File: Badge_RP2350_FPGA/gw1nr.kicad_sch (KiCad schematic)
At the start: 23 parts, among them U2 GW1N-LV9QN88C6_I5_, U6 W25Q32JVSS

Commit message: modify usb and flash connections
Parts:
- added R19: 4.7K, Resistor_THT:R_Axial_DIN0204_L3.6mm_D1.6mm_P1.90mm_Vertical, symbol Device:R
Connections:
- net GND: now also R19.1
- net TCK: now also R19.2
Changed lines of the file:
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@@
 		(rev "v1.0")
 		(company "SemiTO-V, RISC-V Student Team")
-		(comment 3 "License: CERN-OHL-W")
+		(comment 3 "License: CERN-OHL-W-2.0")
 		(comment 4 "Authors: Tan Siret Akıncı, Alessandro Bochino, Carlo Bendelli, Arianna Bruno")
 	)
@@
 	(wire
 		(pts
+			(xy 77.47 80.01) (xy 77.47 83.82)
+		)
+		(stroke
+			(width 0)
+			(type default)
+		)
+	)
+	(wire
+		(pts
 			(xy 166.37 43.18) (xy 179.07 43.18)
 		)
@@
 	(wire
 		(pts
+			(xy 77.47 68.58) (xy 77.47 72.39)
+		)
+		(stroke
+			(width 0)
+			(type default)
+		)
+	)
+	(wire
+		(pts
 			(xy 237.49 34.29) (xy 237.49 44.45)
 		)
@@
 	(wire
 		(pts
-			(xy 86.36 68.58) (xy 100.33 68.58)
+			(xy 77.47 68.58) (xy 100.33 68.58)
 		)
 		(stroke
@@
 	)
 	(label "TCK"
-		(at 86.36 68.58 0)
+		(at 77.47 68.58 0)
 		(effects
 			(font
@@
 	)
 	(symbol
+		(lib_id "power:GND")
+		(at 77.47 83.82 0)
+		(unit 1)
+		(body_style 1)
+		(exclude_from_sim no)
+		(in_bom yes)
+		(on_board yes)
+		(in_pos_files yes)
+		(dnp no)
+		(property "Reference" "#PWR053"
+			(at 77.47 90.17 0)
+			(hide yes)
+			(show_name no)
+			(do_not_autoplace no)
+			(effects
+				(font
+					(size 1.27 1.27)
+				)
+			)
+		)
+		(property "Value" "GND"
+			(at 73.66 85.09 0)
+			(show_name no)
+			(do_not_autoplace no)
+			(effects
+				(font
+					(size 1.27 1.27)
+				)
+			)
+		)
+		(property "Footprint" ""
+			(at 77.47 83.82 0)
+			(hide yes)
+			(show_name no)
+			(do_not_autoplace no)
+			(effects
+				(font
+					(size 1.27 1.27)
+				)
+			)
+		)
+		(property "Datasheet" ""
+			(at 77.47 83.82 0)
+			(hide yes)
+			(show_name no)
+			(do_not_autoplace no)
+			(effects
+				(font
+					(size 1.27 1.27)
+				)
+			)
+		)
+		(property "Description" ""
+			(at 77.47 83.82 0)
+			(show_name no)
+			(do_not_autoplace no)
+			(effects
+				(font
+					(size 1.27 1.27)
+				)
+			)
+		)
+		(pin "1"
+		)
+		(instances
+			(project "Badge_RP2350_FPGA"
+				(path "/0ce87b49-0553-4a87-87c1-84e31180901e/2d8d0ad2-8268-4696-bbfb-79e633c29f55"
+					(reference "#PWR053")
+					(unit 1)
+				)
+			)
+		)
+	)
+	(symbol
 		(lib_id "Memory_Flash:W25Q32JVSS")
 		(at 245.11 132.08 0)
@@
 					(unit 1)
 				)
+			)
+		)
+	)
+	(symbol
+		(lib_id "Device:R")
+		(at 77.47 76.2 180)
+		(unit 1)
+		(body_style 1)
+		(exclude_from_sim no)
+		(in_bom yes)
+		(on_board yes)
+		(in_pos_files yes)
+		(dnp no)
+		(fields_autoplaced yes)
+		(property "Reference" "R19"
+			(at 80.01 74.9299 0)
+			(show_name no)
+			(do_not_autoplace no)
+			(effects
+				(font
+					(size 1.27 1.27)
+				)
+				(justify right)
+			)
+		)
+		(property "Value" "4.7K"
+			(at 80.01 77.4699 0)
+			(show_name no)
+			(do_not_autoplace no)
+			(effects
+				(font
+					(size 1.27 1.27)
+				)
+				(justify right)
+			)
+		)
+		(property "Footprint" "Resistor_THT:R_Axial_DIN0204_L3.6mm_D1.6mm_P1.90mm_Vertical"
+			(at 79.248 76.2 90)
+			(hide yes)
+			(show_name no)
+			(do_not_autoplace no)
+			(effects
+				(font
+					(size 1.27 1.27)
+				)
+			)
+		)
+		(property "Datasheet" ""
+			(at 77.47 76.2 0)
+			(hide yes)
+			(show_name no)
+			(do_not_autoplace no)
+			(effects
+				(font
+					(size 1.27 1.27)
+				)
+			)
+		)
+		(property "Description" "Resistor"
+			(at 77.47 76.2 0)
+			(hide yes)
+			(show_name no)
+			(do_not_autoplace no)
+			(effects
+				(font
+					(size 1.27 1.27)
+				)
+			)
+		)
+		(pin "1"
+		)
+		(pin "2"
+		)
+		(instances
+			(project "Badge_RP2350_FPGA"
+				(path "/0ce87b49-0553-4a87-87c1-84e31180901e/2d8d0ad2-8268-4696-bbfb-79e633c29f55"
+					(reference "R19")
+					(unit 1)
+				)

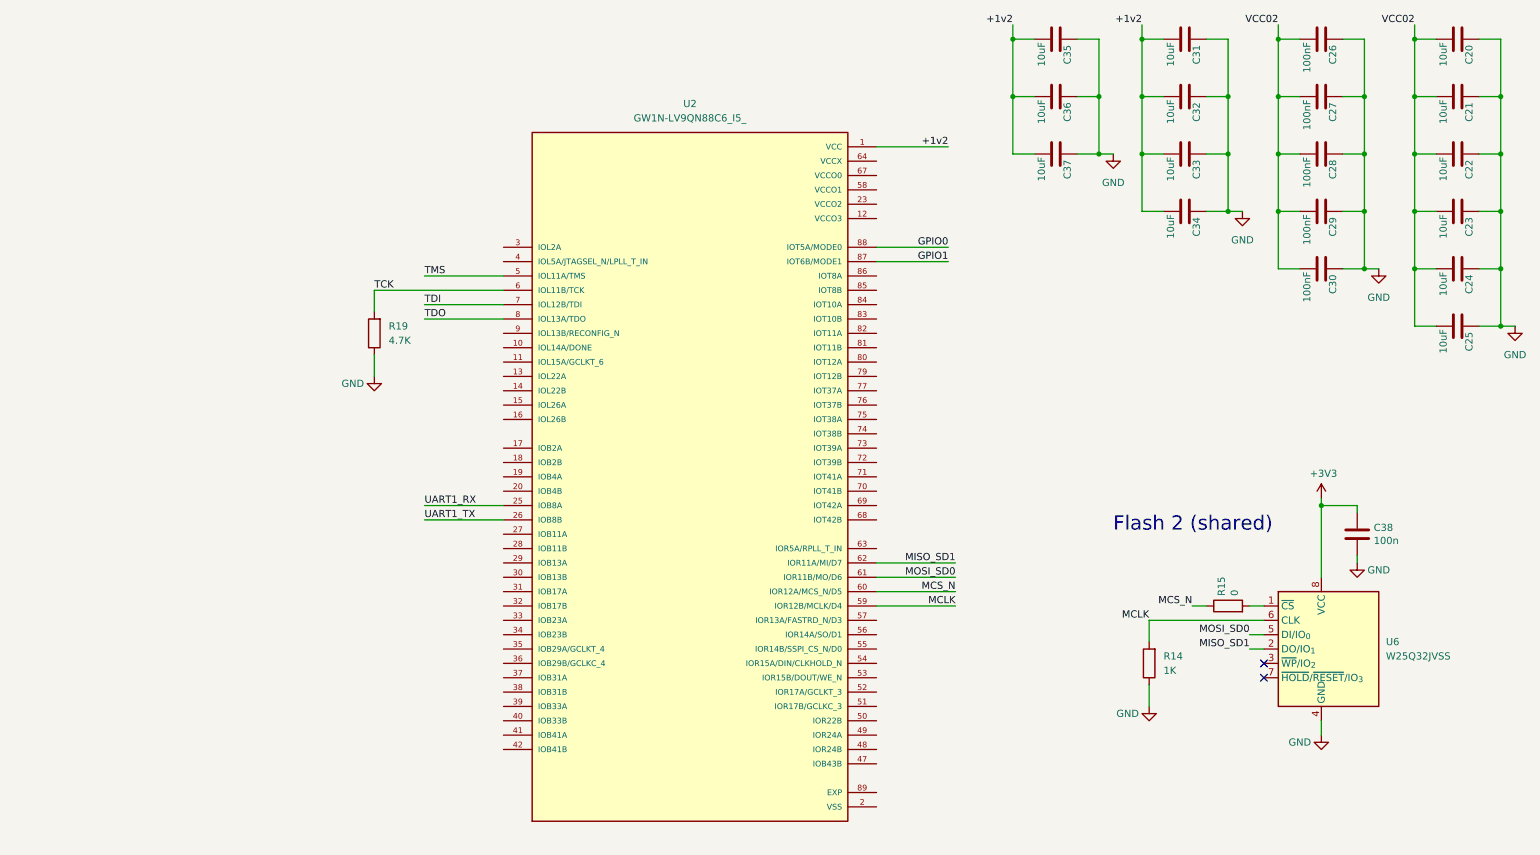
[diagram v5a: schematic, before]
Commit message: edit schematics, add global pins
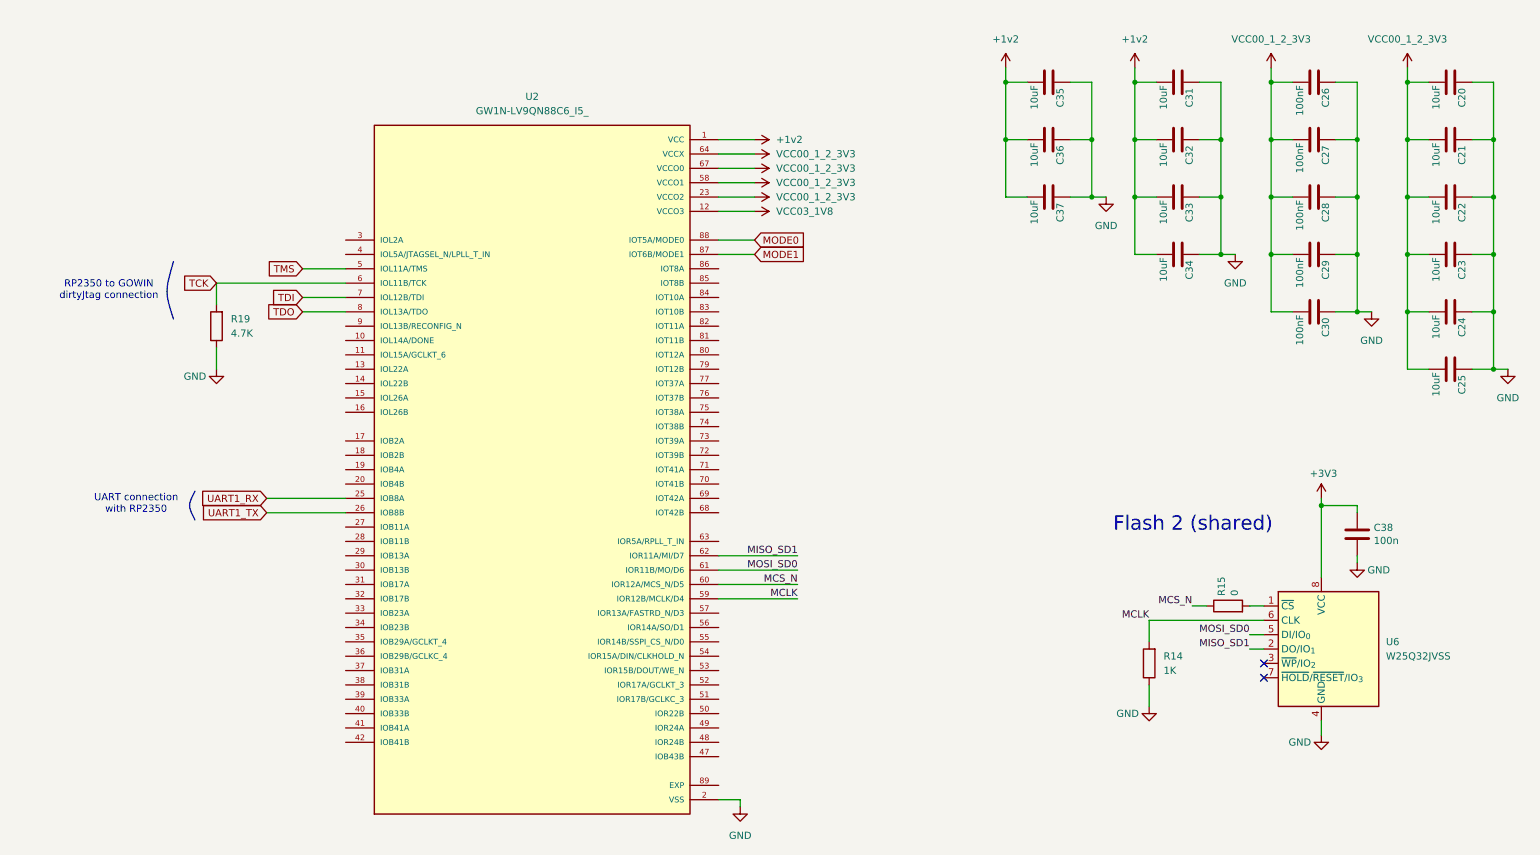
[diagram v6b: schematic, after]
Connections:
- net VCC02 is gone; now on net VCC00_1_2_3V3: C20.2, C21.2, C22.2, C23.2, C24.2, C25.2, C26.2, C27.2, C28.2, C29.2, C30.2
- net VCCO2 is gone; now on net VCC00_1_2_3V3: U2.23 (VCCO2), U2.44 (VCCO2)
- net VCCX is gone; now on net VCC00_1_2_3V3: U2.64 (VCCX), U2.78 (VCCX)
- net VSS is gone; now on net GND: U2.2 (VSS), U2.21 (VSS), U2.24 (VSS), U2.43 (VSS), U2.46 (VSS), U2.65 (VSS)
- net VCC03_1V8: now reaches U2.12 (VCCO3)
- net VCC00_1_2_3V3: now reaches U2.58 (VCCO1)
- net VCC00_1_2_3V3: now also U2.67 (VCCO0)
- net GPIO0 renamed MODE0
- net GPIO1 renamed MODE1
- net VCC renamed +1v2
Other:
- note added: "RP2350 to GOWIN dirtyJtag connection"
- note added: "UART connection with RP2350"
- moved on the sheet: C20, C21, C22, C23, C24, C25, C26, C27, C28, C29, C30, C31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

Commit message: assign all footprints and import to pcb
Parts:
- R14, R19: footprint Resistor_THT:R_Axial_DIN0204_L3.6mm_D1.6mm_P1.90mm_Vertical -> Resistor_SMD:R_0402_1005Metric
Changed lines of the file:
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@@
 			)
 		)
-		(property "Footprint" "Resistor_THT:R_Axial_DIN0204_L3.6mm_D1.6mm_P1.90mm_Vertical"
+		(property "Footprint" "Resistor_SMD:R_0402_1005Metric"
 			(at 216.408 134.62 90)
 			(hide yes)
@@
 			)
 		)
-		(property "Footprint" "Resistor_THT:R_Axial_DIN0204_L3.6mm_D1.6mm_P1.90mm_Vertical"
+		(property "Footprint" "Resistor_SMD:R_0402_1005Metric"
 			(at 51.308 74.93 90)
 			(hide yes)

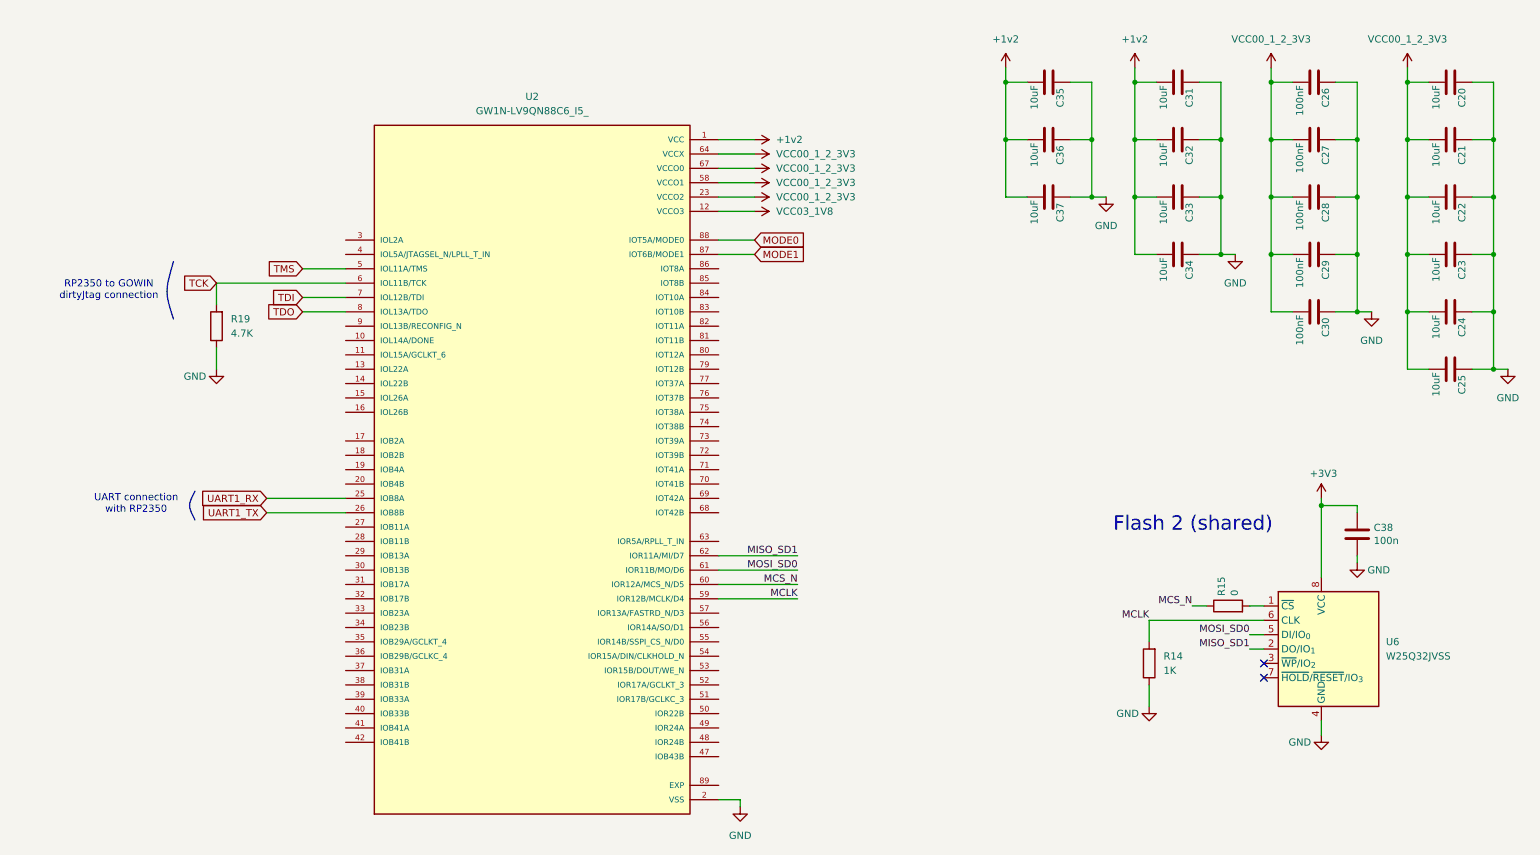
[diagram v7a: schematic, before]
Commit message: add headers and fix voltage references
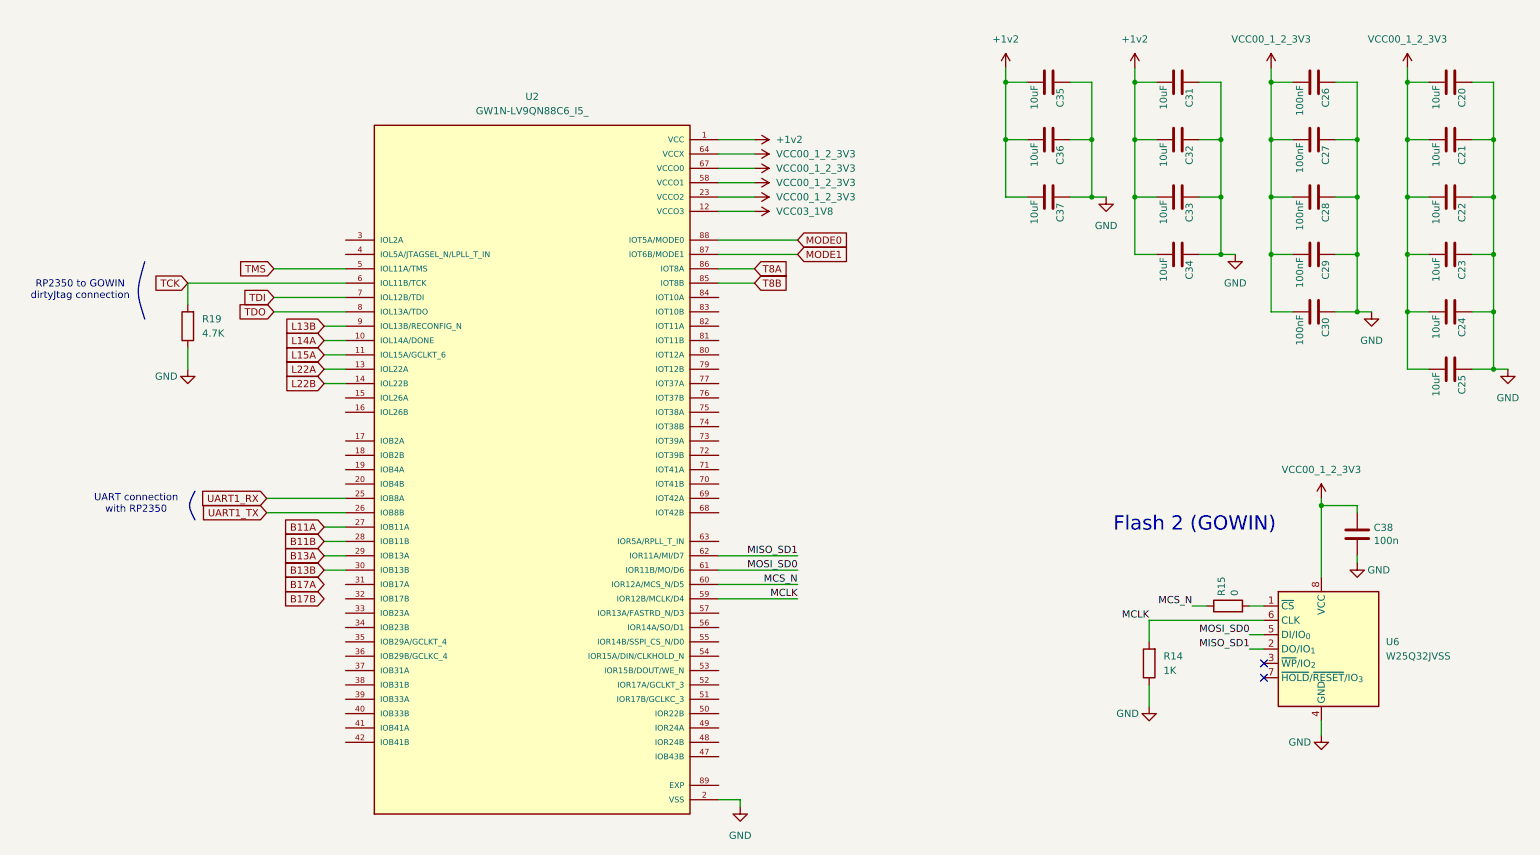
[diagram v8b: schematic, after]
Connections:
- net +3V3 is gone; now on net VCC00_1_2_3V3: C38.1, U6.8 (VCC)
- net L14A: now reaches U2.10 (IOL14A/DONE)
- net L15A: now reaches U2.11 (IOL15A/GCLKT_6)
- net L22A: now reaches U2.13 (IOL22A)
- net L22B: now reaches U2.14 (IOL22B)
- net B11A: now reaches U2.27 (IOB11A)
- net B11B: now reaches U2.28 (IOB11B)
- net B13A: now reaches U2.29 (IOB13A)
- net B13B: now reaches U2.30 (IOB13B)
- net T8B: now reaches U2.85 (IOT8B)
- net T8A: now reaches U2.86 (IOT8A)
- net L13B: now reaches U2.9 (IOL13B/RECONFIG_N)
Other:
- note added: "Flash 2 (GOWIN)"
- note removed: "Flash 2 (shared)"
- moved on the sheet: R19
